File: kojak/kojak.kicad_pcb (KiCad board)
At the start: 2 copper layers, 67 x 27 mm, 27 parts, among them Q1 BC546, Q2 BC546, Q3 BC557, Q4 TIP31C, SW1 MODE

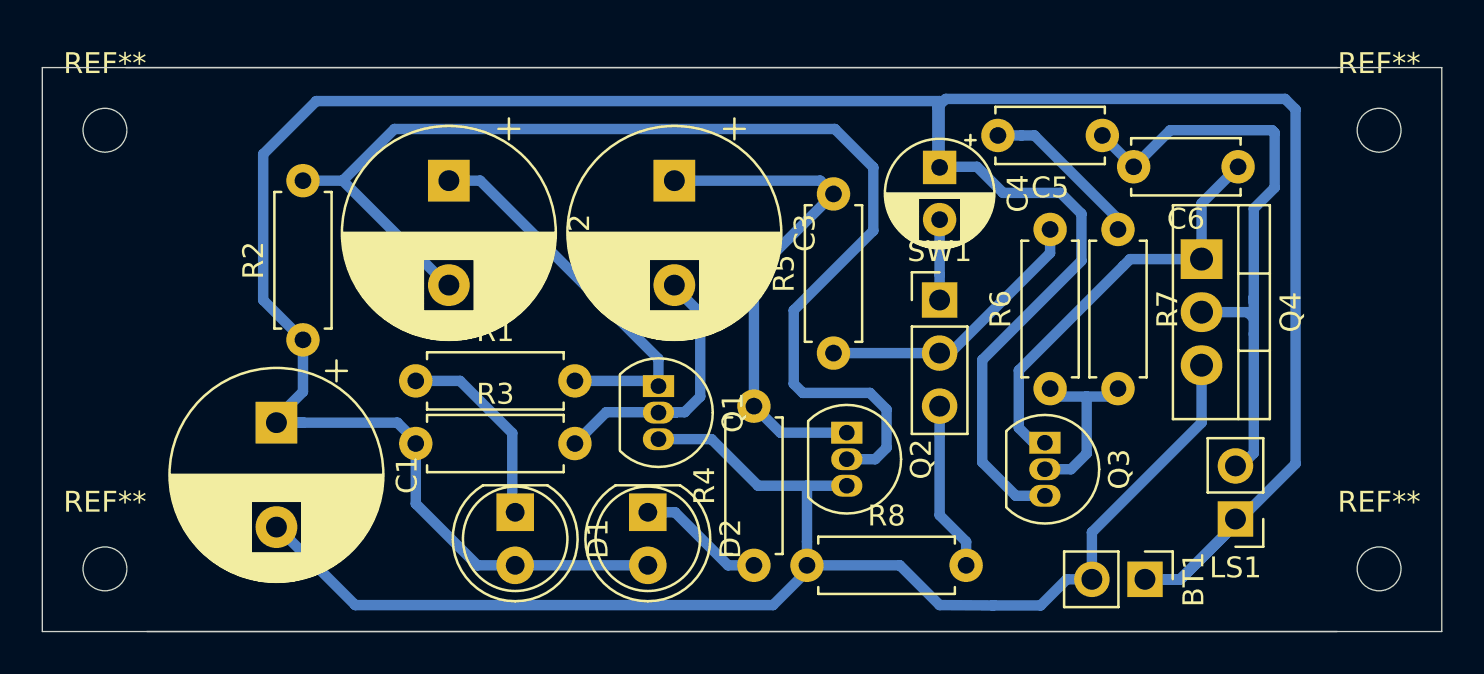
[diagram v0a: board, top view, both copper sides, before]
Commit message: Remove tracks
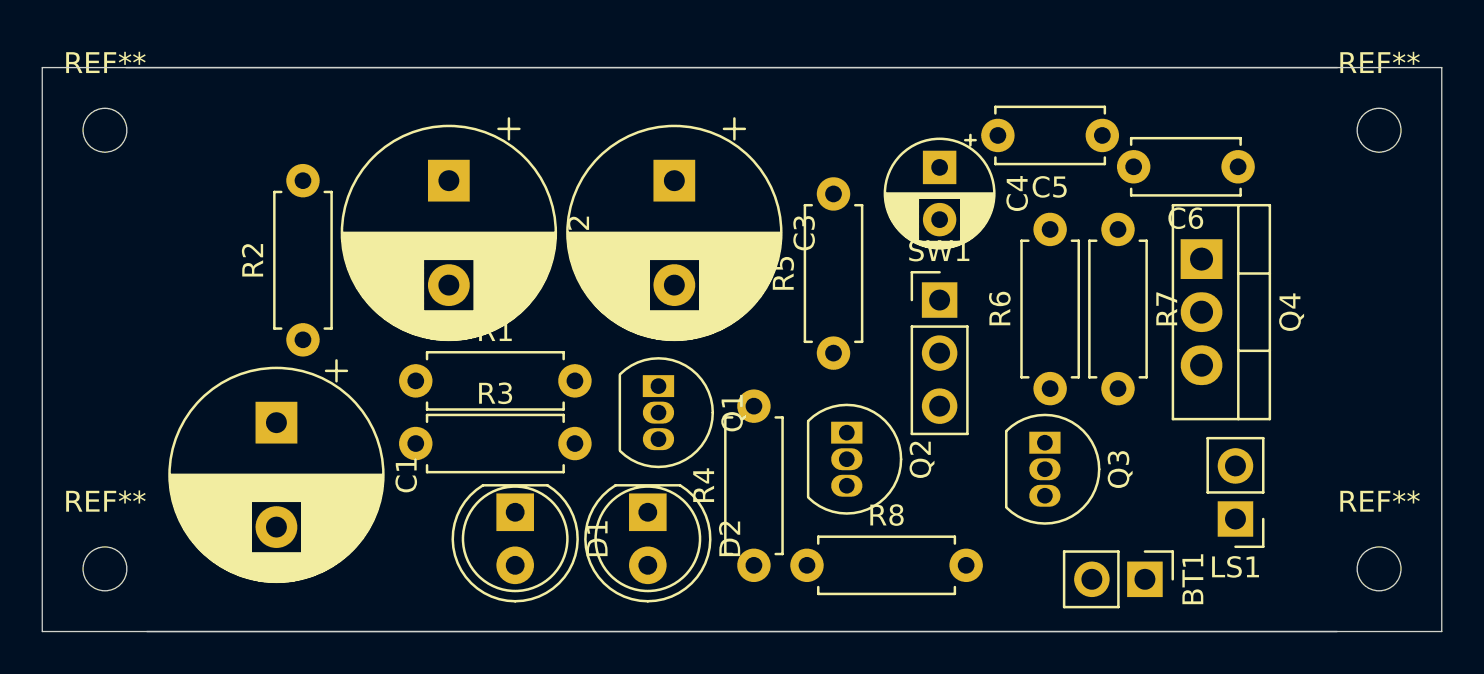
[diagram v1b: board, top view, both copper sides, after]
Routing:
- net VCC: track 153.0 -> 0.00 mm
- net GND: track 68.4 -> 0.00 mm
- net Net-(C2-Pad2): track 57.2 -> 0.00 mm
- net Net-(C5-Pad1): track 29.4 -> 0.00 mm
- net MV_OUT: track 24.0 -> 0.00 mm
- net Net-(C6-Pad1): track 20.4 -> 0.00 mm
- net Net-(C2-Pad1): track 19.0 -> 0.00 mm
- net PITCH: track 13.5 -> 0.00 mm
- net Net-(C3-Pad2): track 13.0 -> 0.00 mm
- net Net-(D1-Pad1): track 9.41 -> 0.00 mm
- net Net-(Q3-Pad2): track 8.42 -> 0.00 mm
- net Net-(R8-Pad2): track 8.15 -> 0.00 mm
- net Net-(C5-Pad2): track 7.91 -> 0.00 mm
- net Net-(D2-Pad1): track 6.13 -> 0.00 mm
- net Net-(C4-Pad2): track 3.81 -> 0.00 mm
